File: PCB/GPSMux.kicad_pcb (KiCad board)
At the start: 2 copper layers, 20 x 26 mm, 20 parts, among them P1 ICSP, P2 GPS1, P3 GPS2, P4 LLU, U1 CY8C27143-24PXI, U2 ADM3101EARQZ

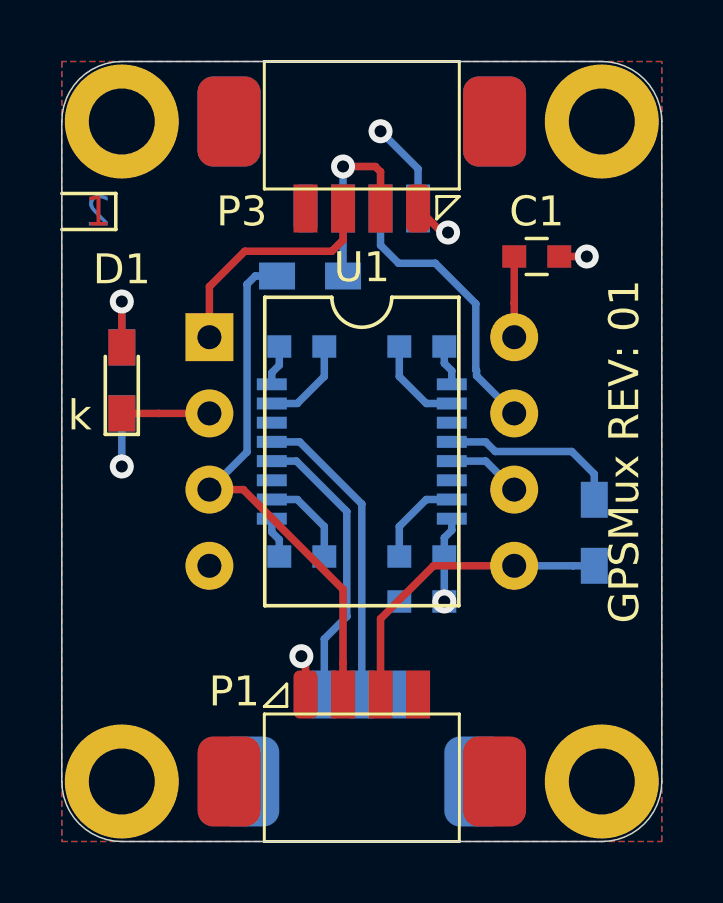
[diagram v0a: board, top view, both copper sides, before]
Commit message: Updated to kicad 8.0
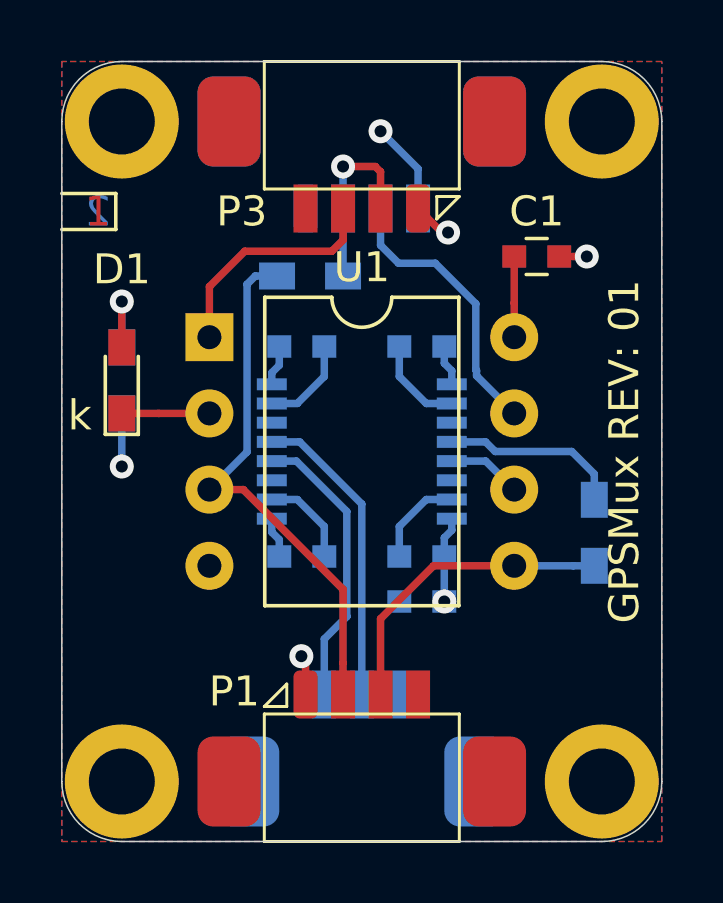
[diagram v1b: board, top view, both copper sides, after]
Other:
- net class Default removed
